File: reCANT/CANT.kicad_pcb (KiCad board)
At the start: 4 copper layers, 82 x 49.1 mm, 74 parts, among them J1 USB_C_Receptacle_USB2.0, J2 Conn_02x08_Odd_Even, J3 Screw_Terminal_01x04, J4 Screw_Terminal_01x02, P1 SWD, SW1 SW_SPST, U1 USB3343, U10 DSC1001, U2 LD1117S33TR, U3 STM32H743VITx, U4 MCP2558FD-xSN, U5 MCP2558FD-xSN, U6 74LVC1G66, U7 74LVC1G66, U8 SN74LVC1G14DBV, U9 ST485EBDR

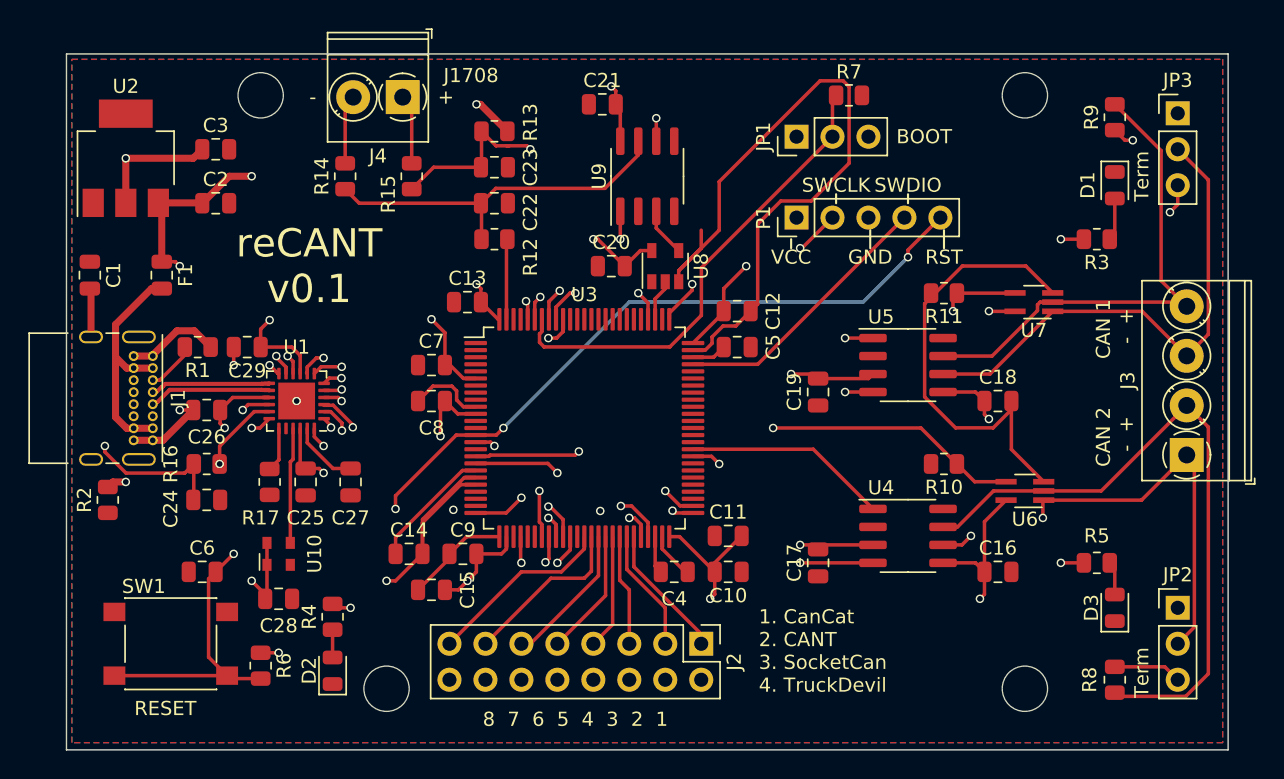
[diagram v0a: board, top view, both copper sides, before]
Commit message: Added test points for debugging USB. Fixed impedence on USB traces to be correct for JLCPCBs JLC7628 buildup
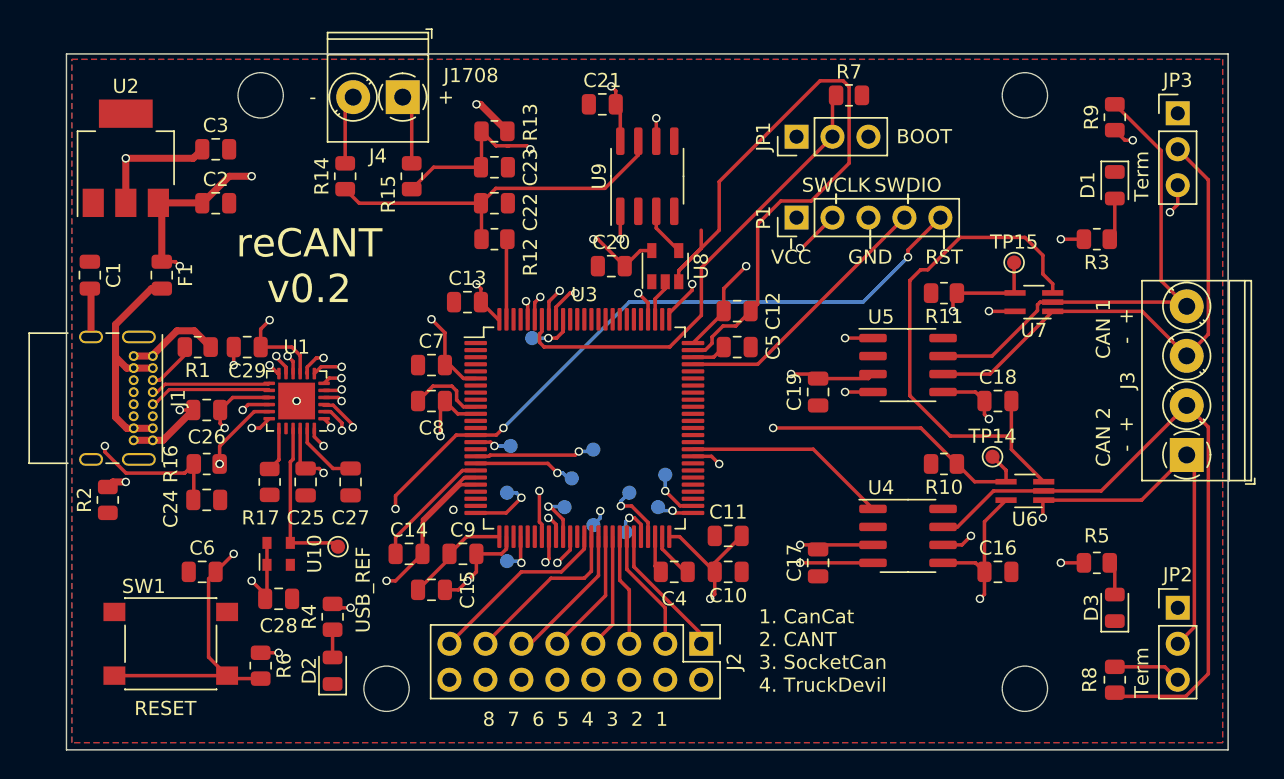
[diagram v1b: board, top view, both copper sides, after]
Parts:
- added TP14: TestPoint, TestPoint:TestPoint_Pad_D1.0mm, F.Cu at (80.3, 90.9)
- added TP15: TestPoint, TestPoint:TestPoint_Pad_D1.0mm, F.Cu at (81.8, 77.2)
- added USB_CK: TestPoint, TestPoint:TestPoint_Pad_D1.0mm, B.Cu at (46.0, 98.3)
- added USB_D0: TestPoint, TestPoint:TestPoint_Pad_D1.0mm, B.Cu at (46.0, 93.5)
- added USB_D1: TestPoint, TestPoint:TestPoint_Pad_D1.0mm, B.Cu at (52.1, 95.8)
- added USB_D2: TestPoint, TestPoint:TestPoint_Pad_D1.0mm, B.Cu at (50.0, 94.5)
- added USB_D3: TestPoint, TestPoint:TestPoint_Pad_D1.0mm, B.Cu at (54.4, 96.3)
- added USB_D4: TestPoint, TestPoint:TestPoint_Pad_D1.0mm, B.Cu at (54.6, 93.5)
- added USB_D5: TestPoint, TestPoint:TestPoint_Pad_D1.0mm, B.Cu at (56.6, 94.5)
- added USB_D6: TestPoint, TestPoint:TestPoint_Pad_D1.0mm, B.Cu at (57.1, 92.2)
- added USB_D7: TestPoint, TestPoint:TestPoint_Pad_D1.0mm, B.Cu at (47.8, 82.5)
- added USB_DIR: TestPoint, TestPoint:TestPoint_Pad_D1.0mm, B.Cu at (52.1, 90.4)
- added USB_NXT: TestPoint, TestPoint:TestPoint_Pad_D1.0mm, B.Cu at (50.5, 92.5)
- added USB_REF: TestPoint, TestPoint:TestPoint_Pad_D1.0mm, F.Cu at (34.0, 97.3)
- added USB_STP: TestPoint, TestPoint:TestPoint_Pad_D1.0mm, B.Cu at (46.2, 90.2)
- F1: value Polyfuse -> Polyfuse 6v 1A
- U3: value STM32H743VITx -> STM32H733VGTx
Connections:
- J1 pad A8: (no net) -> Net-(J1-PadA8)
- J1 pad B8: (no net) -> Net-(J1-PadB8)
- JP1 pad 1: (no net) -> Net-(JP1-Pad1)
- JP2 pad 1: (no net) -> Net-(JP2-Pad1)
- JP3 pad 1: (no net) -> Net-(JP3-Pad1)
- U1 pad 20: (no net) -> Net-(U1-Pad20)
- U3 pad 1: (no net) -> Net-(U3-Pad1)
- U3 pad 12: (no net) -> Net-(U3-Pad12)
- U3 pad 13: (no net) -> Net-(U3-Pad13)
- U3 pad 16: (no net) -> Net-(U3-Pad16)
- U3 pad 2: (no net) -> Net-(U3-Pad2)
- U3 pad 22: (no net) -> Net-(U3-Pad22)
- U3 pad 23: (no net) -> Net-(U3-Pad23)
- U3 pad 24: (no net) -> Net-(U3-Pad24)
- U3 pad 28: (no net) -> Net-(U3-Pad28)
- U3 pad 3: (no net) -> Net-(U3-Pad3)
- U3 pad 30: (no net) -> Net-(U3-Pad30)
- U3 pad 31: (no net) -> Net-(U3-Pad31)
- U3 pad 37: (no net) -> Net-(U3-Pad37)
- U3 pad 4: (no net) -> Net-(U3-Pad4)
- U3 pad 5: (no net) -> Net-(U3-Pad5)
- U3 pad 53: (no net) -> Net-(U3-Pad53)
- U3 pad 54: (no net) -> Net-(U3-Pad54)
- U3 pad 55: (no net) -> Net-(U3-Pad55)
- U3 pad 56: (no net) -> Net-(U3-Pad56)
- U3 pad 57: (no net) -> Net-(U3-Pad57)
- U3 pad 58: (no net) -> Net-(U3-Pad58)
- U3 pad 61: (no net) -> Net-(U3-Pad61)
- U3 pad 62: (no net) -> Net-(U3-Pad62)
- U3 pad 63: (no net) -> Net-(U3-Pad63)
- U3 pad 64: (no net) -> Net-(U3-Pad64)
- U3 pad 65: (no net) -> Net-(U3-Pad65)
- U3 pad 66: (no net) -> Net-(U3-Pad66)
- U3 pad 67: (no net) -> Net-(U3-Pad67)
- U3 pad 68: (no net) -> Net-(U3-Pad68)
- U3 pad 69: (no net) -> Net-(U3-Pad69)
- U3 pad 7: (no net) -> Net-(U3-Pad7)
- U3 pad 70: (no net) -> Net-(U3-Pad70)
- U3 pad 71: (no net) -> Net-(U3-Pad71)
- U3 pad 77: (no net) -> Net-(U3-Pad77)
- U3 pad 8: (no net) -> Net-(U3-Pad8)
- U3 pad 80: (no net) -> Net-(U3-Pad80)
- U3 pad 81: (no net) -> Net-(U3-Pad81)
- U3 pad 82: (no net) -> Net-(U3-Pad82)
- U3 pad 83: (no net) -> Net-(U3-Pad83)
- U3 pad 84: (no net) -> Net-(U3-Pad84)
- U3 pad 85: (no net) -> Net-(U3-Pad85)
- U3 pad 86: (no net) -> Net-(U3-Pad86)
- U3 pad 87: (no net) -> Net-(U3-Pad87)
- U3 pad 88: (no net) -> Net-(U3-Pad88)
- U3 pad 89: (no net) -> Net-(U3-Pad89)
- U3 pad 9: (no net) -> Net-(U3-Pad9)
- U3 pad 90: (no net) -> Net-(U3-Pad90)
- U3 pad 97: (no net) -> Net-(U3-Pad97)
- U3 pad 98: (no net) -> Net-(U3-Pad98)
- U8 pad 1: (no net) -> Net-(U8-Pad1)
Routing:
- net GND: track 132.2 -> 137.1 mm
- net Net-(TP1-Pad1): track 8.16 -> 11.6 mm
- net CAN1_SHORT: track 36.2 -> 38.4 mm
- net CAN3_SHORT: track 38.6 -> 40.7 mm
- net USB_D7: track 38.6 -> 39.9 mm
- net USB_NXT: track 34.5 -> 35.8 mm
- net USB_D2: track 35.7 -> 36.9 mm
- net USB_D1: track 35.3 -> 36.5 mm
- net USB_D4: track 35.1 -> 36.3 mm
- net USB_D0: track 35.2 -> 36.4 mm
- net USB_STP: track 36.4 -> 37.6 mm
- net USB_D6: track 36.8 -> 38.0 mm
- net USB_D5: track 36.1 -> 37.3 mm
- net USB_D3: track 35.6 -> 36.7 mm
- net USB_DIR: track 35.5 -> 36.6 mm
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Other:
- net class USB Data: trace_width 0.25 -> 0.2286
- board text added: "reCANT v0.2"
- board text removed: "reCANT v0.1"
